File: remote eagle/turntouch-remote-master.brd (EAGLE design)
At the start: 36.8 x 36.8 mm, 17 parts, among them J1 TC2030-JLINK-NL, Q1 CRYSTAL.ABS07, U1 MDBT40SMD

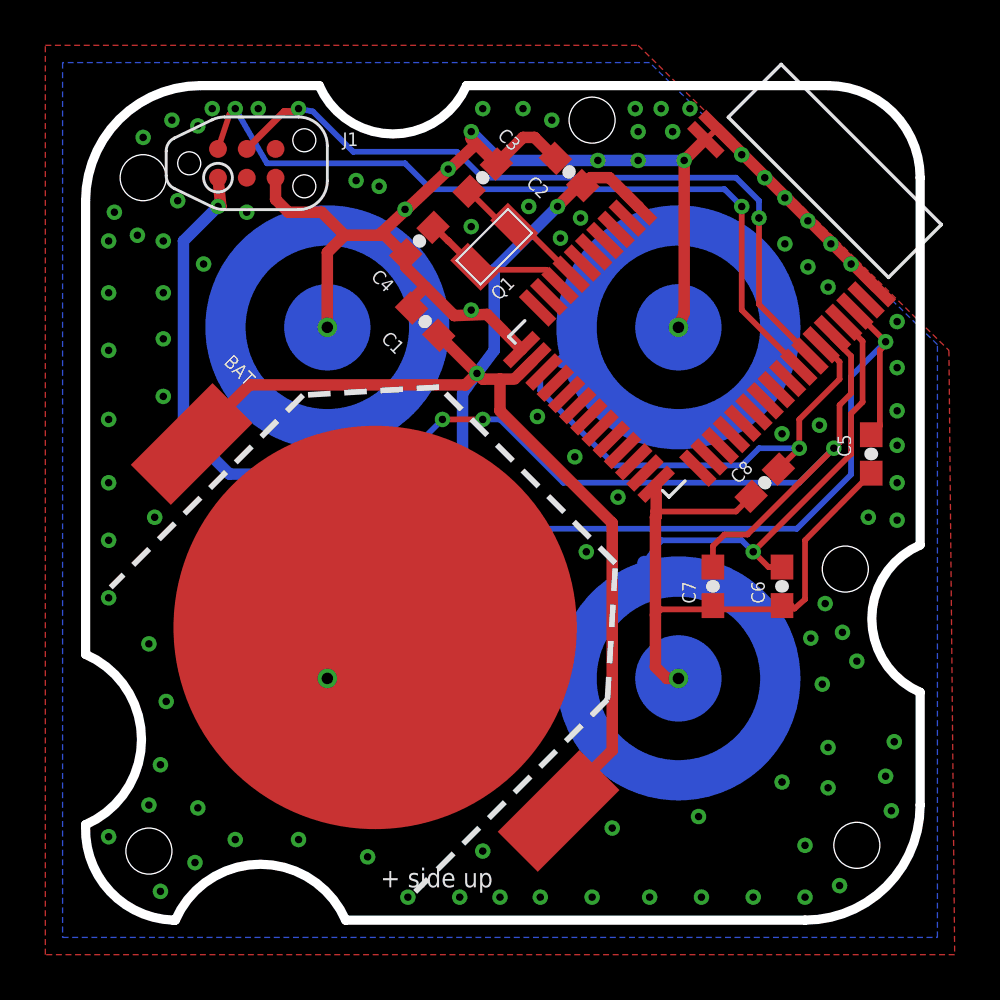
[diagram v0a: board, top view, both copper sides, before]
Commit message: Rev 35: moving board mounts around.
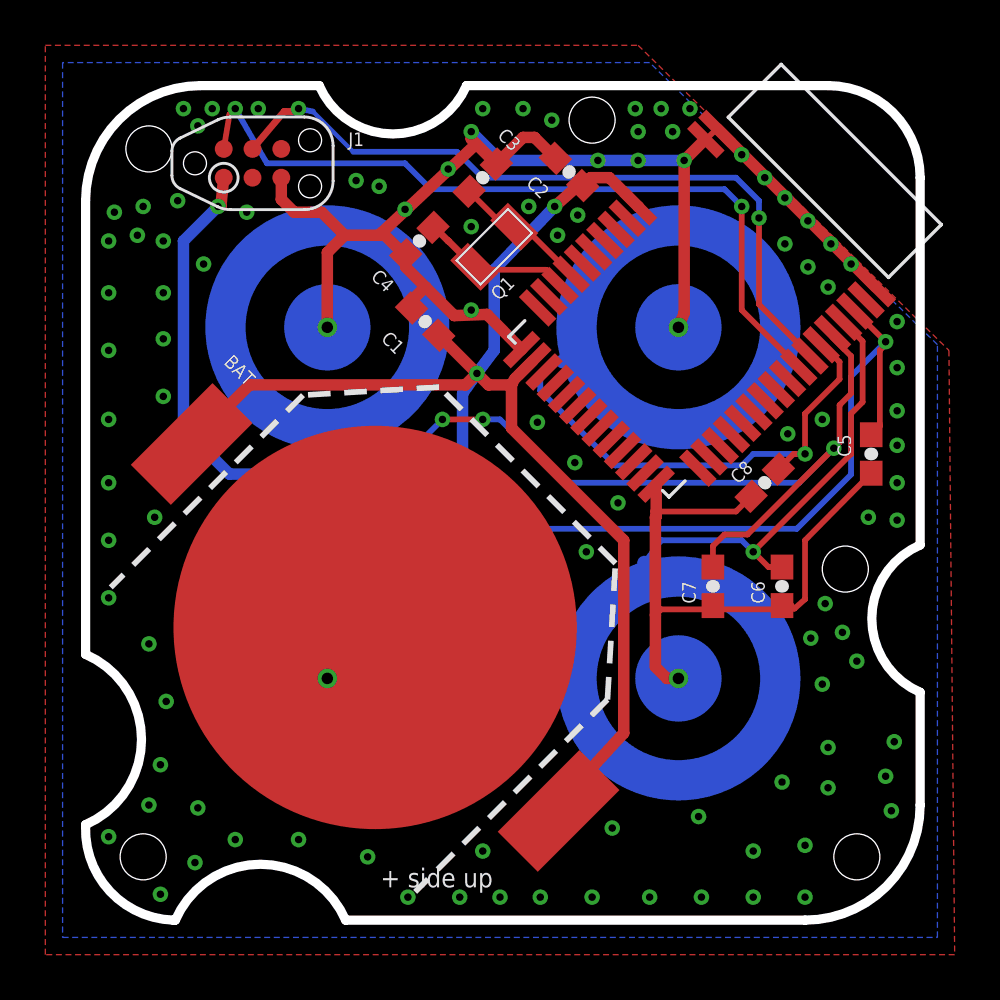
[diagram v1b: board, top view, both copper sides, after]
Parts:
- moved J1 0.25 mm to (7.37, 33.4)
